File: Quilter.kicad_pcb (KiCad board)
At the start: 2 copper layers, 62 x 56 mm, 32 parts, among them J1 IO, J2 Power, J3 Power_In, U1 SSI2144, U2 TL072

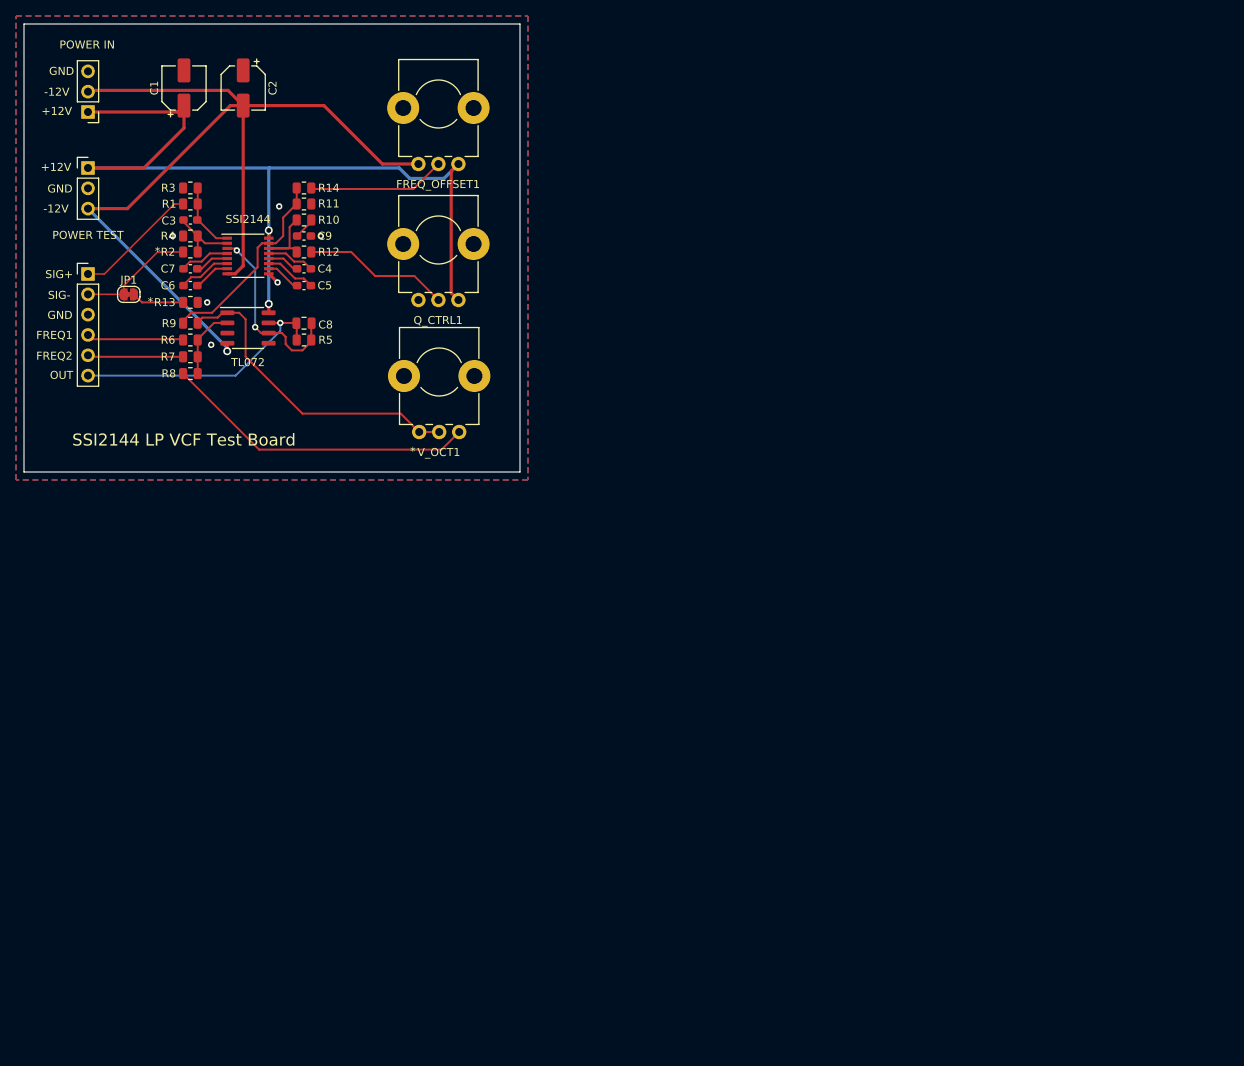
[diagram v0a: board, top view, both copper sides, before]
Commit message: Started component PCB layout
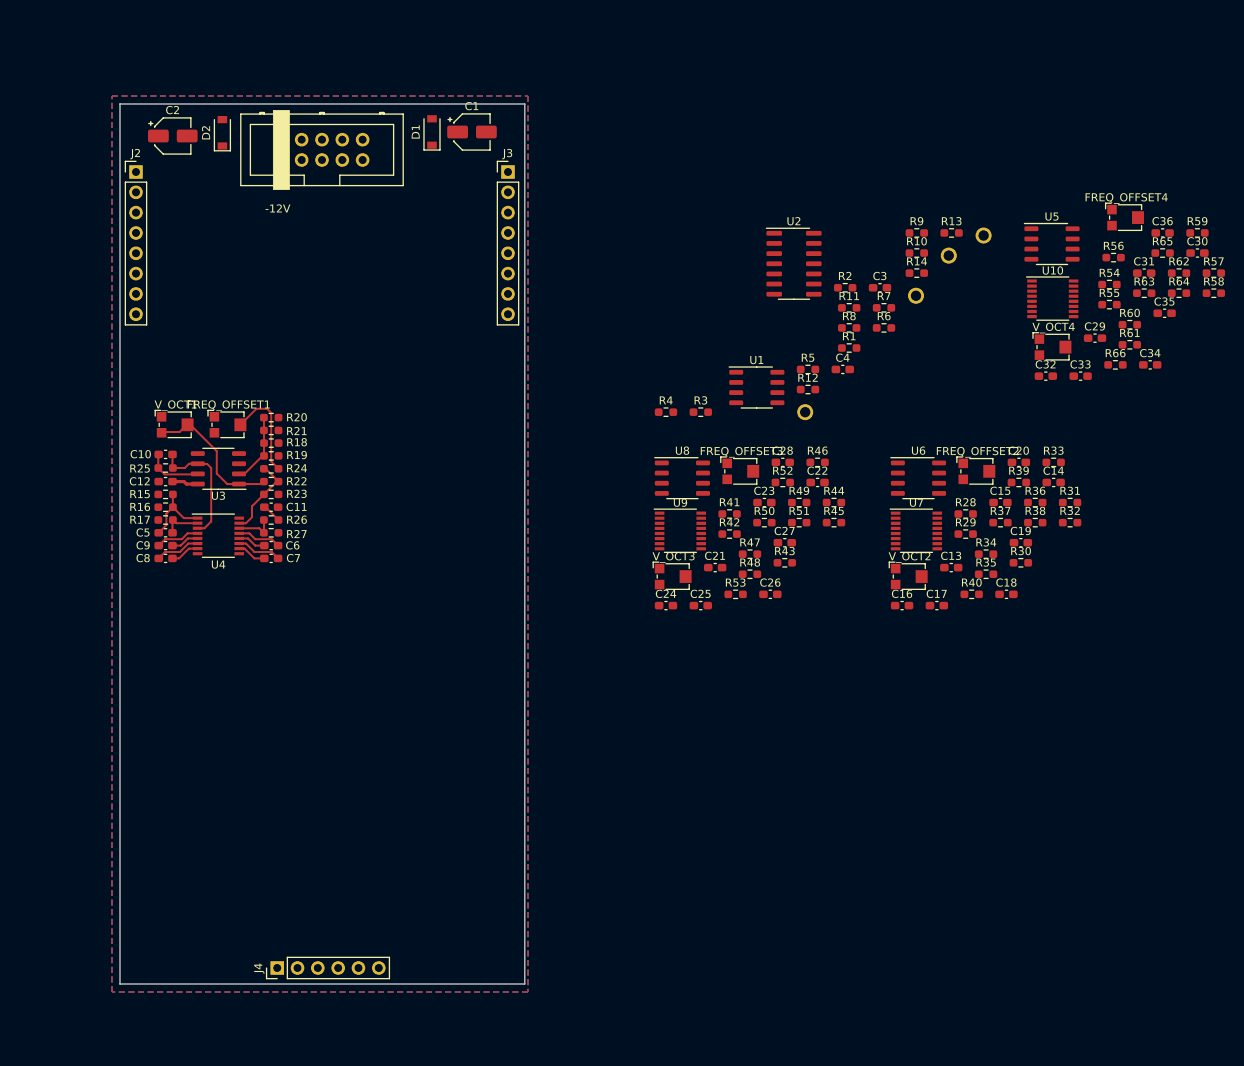
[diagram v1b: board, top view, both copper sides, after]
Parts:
- removed JP1: Jumper_2_Bridged, Jumper:SolderJumper-2_P1.3mm_Bridged_RoundedPad1.0x1.5mm
- removed Q_CTRL1: 10k, Custom_Footprints:Alpha_9mm_Potentiometer_Aligned
- added C10: 100pF, Capacitor_SMD:C_0603_1608Metric_Pad1.08x0.95mm_HandSolder, F.Cu at (55.7, 93.8)
- added C11: 10nF, Capacitor_SMD:C_0603_1608Metric_Pad1.08x0.95mm_HandSolder, F.Cu at (68.9, 100.4)
- added C12: 1uF, Capacitor_SMD:C_0603_1608Metric_Pad1.08x0.95mm_HandSolder, F.Cu at (55.7, 97.2)
- added C13: 3.3nF, Capacitor_SMD:C_0603_1608Metric_Pad1.08x0.95mm_HandSolder, F.Cu at (153.9, 108.0)
- added C14: 6.8nF, Capacitor_SMD:C_0603_1608Metric_Pad1.08x0.95mm_HandSolder, F.Cu at (166.7, 97.3)
- added C15: 6.8nF, Capacitor_SMD:C_0603_1608Metric_Pad1.08x0.95mm_HandSolder, F.Cu at (160.1, 99.8)
- added C16: 6.8nF, Capacitor_SMD:C_0603_1608Metric_Pad1.08x0.95mm_HandSolder, F.Cu at (147.8, 112.7)
- added C17: 560pF, Capacitor_SMD:C_0603_1608Metric_Pad1.08x0.95mm_HandSolder, F.Cu at (152.1, 112.7)
- added C18: 100pF, Capacitor_SMD:C_0603_1608Metric_Pad1.08x0.95mm_HandSolder, F.Cu at (160.8, 111.3)
- added C19: 10nF, Capacitor_SMD:C_0603_1608Metric_Pad1.08x0.95mm_HandSolder, F.Cu at (162.6, 104.8)
- added C20: 1uF, Capacitor_SMD:C_0603_1608Metric_Pad1.08x0.95mm_HandSolder, F.Cu at (162.4, 94.8)
- added C21: 3.3nF, Capacitor_SMD:C_0603_1608Metric_Pad1.08x0.95mm_HandSolder, F.Cu at (124.4, 108.0)
- added C22: 6.8nF, Capacitor_SMD:C_0603_1608Metric_Pad1.08x0.95mm_HandSolder, F.Cu at (137.2, 97.3)
- added C23: 6.8nF, Capacitor_SMD:C_0603_1608Metric_Pad1.08x0.95mm_HandSolder, F.Cu at (130.6, 99.8)
- added C24: 6.8nF, Capacitor_SMD:C_0603_1608Metric_Pad1.08x0.95mm_HandSolder, F.Cu at (118.2, 112.7)
- added C25: 560pF, Capacitor_SMD:C_0603_1608Metric_Pad1.08x0.95mm_HandSolder, F.Cu at (122.6, 112.7)
- added C26: 100pF, Capacitor_SMD:C_0603_1608Metric_Pad1.08x0.95mm_HandSolder, F.Cu at (131.3, 111.3)
- added C27: 10nF, Capacitor_SMD:C_0603_1608Metric_Pad1.08x0.95mm_HandSolder, F.Cu at (133.1, 104.8)
- added C28: 1uF, Capacitor_SMD:C_0603_1608Metric_Pad1.08x0.95mm_HandSolder, F.Cu at (132.8, 94.8)
- added C29: 3.3nF, Capacitor_SMD:C_0603_1608Metric_Pad1.08x0.95mm_HandSolder, F.Cu at (171.9, 79.3)
- added C30: 6.8nF, Capacitor_SMD:C_0603_1608Metric_Pad1.08x0.95mm_HandSolder, F.Cu at (184.7, 68.6)
- added C31: 6.8nF, Capacitor_SMD:C_0603_1608Metric_Pad1.08x0.95mm_HandSolder, F.Cu at (178.0, 71.1)
- added C32: 6.8nF, Capacitor_SMD:C_0603_1608Metric_Pad1.08x0.95mm_HandSolder, F.Cu at (165.7, 84.0)
- added C33: 560pF, Capacitor_SMD:C_0603_1608Metric_Pad1.08x0.95mm_HandSolder, F.Cu at (170.1, 84.0)
- added C34: 100pF, Capacitor_SMD:C_0603_1608Metric_Pad1.08x0.95mm_HandSolder, F.Cu at (178.8, 82.6)
- added C35: 10nF, Capacitor_SMD:C_0603_1608Metric_Pad1.08x0.95mm_HandSolder, F.Cu at (180.6, 76.2)
- added C36: 1uF, Capacitor_SMD:C_0603_1608Metric_Pad1.08x0.95mm_HandSolder, F.Cu at (180.3, 66.1)
- added D1: 1N5819, Diode_SMD:D_SOD-123, F.Cu at (89.0, 53.5)
- added D2: 1N5819, Diode_SMD:D_SOD-123, F.Cu at (62.8, 53.6)
- added FREQ_OFFSET2: 50k, Potentiometer_SMD:Potentiometer_Bourns_TC33X_Vertical, F.Cu at (157.2, 95.9)
- added FREQ_OFFSET3: 50k, Potentiometer_SMD:Potentiometer_Bourns_TC33X_Vertical, F.Cu at (127.7, 95.9)
- added FREQ_OFFSET4: 50k, Potentiometer_SMD:Potentiometer_Bourns_TC33X_Vertical, F.Cu at (175.8, 64.2)
- added J4: IO, Connector_PinHeader_2.54mm:PinHeader_1x06_P2.54mm_Vertical, F.Cu at (69.7, 158.0)
- added R15: 68.1k, Resistor_SMD:R_0603_1608Metric_Pad0.98x0.95mm_HandSolder, F.Cu at (55.7, 98.8)
- added R16: 200, Resistor_SMD:R_0603_1608Metric_Pad0.98x0.95mm_HandSolder, F.Cu at (55.7, 100.4)
- added R17: 200, Resistor_SMD:R_0603_1608Metric_Pad0.98x0.95mm_HandSolder, F.Cu at (55.7, 102.0)
- added R18: 100k, Resistor_SMD:R_0603_1608Metric_Pad0.98x0.95mm_HandSolder, F.Cu at (68.9, 92.4)
- added R19: 100k, Resistor_SMD:R_0603_1608Metric_Pad0.98x0.95mm_HandSolder, F.Cu at (68.9, 94.0)
- added R20: 100k, Resistor_SMD:R_0603_1608Metric_Pad0.98x0.95mm_HandSolder, F.Cu at (68.9, 89.2)
- added R21: 162k, Resistor_SMD:R_0603_1608Metric_Pad0.98x0.95mm_HandSolder, F.Cu at (68.9, 90.8)
- added R22: 100k, Resistor_SMD:R_0603_1608Metric_Pad0.98x0.95mm_HandSolder, F.Cu at (68.9, 97.2)
- added R23: 1k, Resistor_SMD:R_0603_1608Metric_Pad0.98x0.95mm_HandSolder, F.Cu at (68.9, 98.8)
- added R24: 499k, Resistor_SMD:R_0603_1608Metric_Pad0.98x0.95mm_HandSolder, F.Cu at (68.9, 95.6)
- added R25: 33.2k, Resistor_SMD:R_0603_1608Metric_Pad0.98x0.95mm_HandSolder, F.Cu at (55.7, 95.5)
- added R26: 499, Resistor_SMD:R_0603_1608Metric_Pad0.98x0.95mm_HandSolder, F.Cu at (68.9, 102.0)
- added R27: 26.7k, Resistor_SMD:R_0603_1608Metric_Pad0.98x0.95mm_HandSolder, F.Cu at (68.9, 103.6)
- added R28: 68.1k, Resistor_SMD:R_0603_1608Metric_Pad0.98x0.95mm_HandSolder, F.Cu at (155.7, 101.2)
- added R29: 200, Resistor_SMD:R_0603_1608Metric_Pad0.98x0.95mm_HandSolder, F.Cu at (155.7, 103.8)
- added R30: 200, Resistor_SMD:R_0603_1608Metric_Pad0.98x0.95mm_HandSolder, F.Cu at (162.6, 107.3)
- added R31: 100k, Resistor_SMD:R_0603_1608Metric_Pad0.98x0.95mm_HandSolder, F.Cu at (168.8, 99.8)
- added R32: 100k, Resistor_SMD:R_0603_1608Metric_Pad0.98x0.95mm_HandSolder, F.Cu at (168.8, 102.3)
- added R33: 100k, Resistor_SMD:R_0603_1608Metric_Pad0.98x0.95mm_HandSolder, F.Cu at (166.7, 94.8)
- added R34: 162k, Resistor_SMD:R_0603_1608Metric_Pad0.98x0.95mm_HandSolder, F.Cu at (158.3, 106.3)
- added R35: 100k, Resistor_SMD:R_0603_1608Metric_Pad0.98x0.95mm_HandSolder, F.Cu at (158.3, 108.8)
- added R36: 1k, Resistor_SMD:R_0603_1608Metric_Pad0.98x0.95mm_HandSolder, F.Cu at (164.4, 99.8)
- added R37: 499k, Resistor_SMD:R_0603_1608Metric_Pad0.98x0.95mm_HandSolder, F.Cu at (160.1, 102.3)
- added R38: 33.2k, Resistor_SMD:R_0603_1608Metric_Pad0.98x0.95mm_HandSolder, F.Cu at (164.4, 102.3)
- added R39: 499, Resistor_SMD:R_0603_1608Metric_Pad0.98x0.95mm_HandSolder, F.Cu at (162.4, 97.3)
- added R40: 26.7k, Resistor_SMD:R_0603_1608Metric_Pad0.98x0.95mm_HandSolder, F.Cu at (156.5, 111.3)
- added R41: 68.1k, Resistor_SMD:R_0603_1608Metric_Pad0.98x0.95mm_HandSolder, F.Cu at (126.2, 101.2)
- added R42: 200, Resistor_SMD:R_0603_1608Metric_Pad0.98x0.95mm_HandSolder, F.Cu at (126.2, 103.8)
- added R43: 200, Resistor_SMD:R_0603_1608Metric_Pad0.98x0.95mm_HandSolder, F.Cu at (133.1, 107.3)
- added R44: 100k, Resistor_SMD:R_0603_1608Metric_Pad0.98x0.95mm_HandSolder, F.Cu at (139.2, 99.8)
- added R45: 100k, Resistor_SMD:R_0603_1608Metric_Pad0.98x0.95mm_HandSolder, F.Cu at (139.2, 102.3)
- added R46: 100k, Resistor_SMD:R_0603_1608Metric_Pad0.98x0.95mm_HandSolder, F.Cu at (137.2, 94.8)
- added R47: 162k, Resistor_SMD:R_0603_1608Metric_Pad0.98x0.95mm_HandSolder, F.Cu at (128.8, 106.3)
- added R48: 100k, Resistor_SMD:R_0603_1608Metric_Pad0.98x0.95mm_HandSolder, F.Cu at (128.8, 108.8)
- added R49: 1k, Resistor_SMD:R_0603_1608Metric_Pad0.98x0.95mm_HandSolder, F.Cu at (134.9, 99.8)
- added R50: 499k, Resistor_SMD:R_0603_1608Metric_Pad0.98x0.95mm_HandSolder, F.Cu at (130.6, 102.3)
- added R51: 33.2k, Resistor_SMD:R_0603_1608Metric_Pad0.98x0.95mm_HandSolder, F.Cu at (134.9, 102.3)
- added R52: 499, Resistor_SMD:R_0603_1608Metric_Pad0.98x0.95mm_HandSolder, F.Cu at (132.8, 97.3)
- added R53: 26.7k, Resistor_SMD:R_0603_1608Metric_Pad0.98x0.95mm_HandSolder, F.Cu at (127.0, 111.3)
- added R54: 68.1k, Resistor_SMD:R_0603_1608Metric_Pad0.98x0.95mm_HandSolder, F.Cu at (173.7, 72.6)
- added R55: 200, Resistor_SMD:R_0603_1608Metric_Pad0.98x0.95mm_HandSolder, F.Cu at (173.7, 75.1)
- added R56: 200, Resistor_SMD:R_0603_1608Metric_Pad0.98x0.95mm_HandSolder, F.Cu at (174.2, 69.2)
- added R57: 100k, Resistor_SMD:R_0603_1608Metric_Pad0.98x0.95mm_HandSolder, F.Cu at (186.7, 71.1)
- added R58: 100k, Resistor_SMD:R_0603_1608Metric_Pad0.98x0.95mm_HandSolder, F.Cu at (186.7, 73.7)
- added R59: 100k, Resistor_SMD:R_0603_1608Metric_Pad0.98x0.95mm_HandSolder, F.Cu at (184.7, 66.1)
- added R60: 162k, Resistor_SMD:R_0603_1608Metric_Pad0.98x0.95mm_HandSolder, F.Cu at (176.2, 77.6)
- added R61: 100k, Resistor_SMD:R_0603_1608Metric_Pad0.98x0.95mm_HandSolder, F.Cu at (176.2, 80.1)
- added R62: 1k, Resistor_SMD:R_0603_1608Metric_Pad0.98x0.95mm_HandSolder, F.Cu at (182.4, 71.1)
- added R63: 499k, Resistor_SMD:R_0603_1608Metric_Pad0.98x0.95mm_HandSolder, F.Cu at (178.0, 73.7)
- added R64: 33.2k, Resistor_SMD:R_0603_1608Metric_Pad0.98x0.95mm_HandSolder, F.Cu at (182.4, 73.7)
- added R65: 499, Resistor_SMD:R_0603_1608Metric_Pad0.98x0.95mm_HandSolder, F.Cu at (180.3, 68.6)
- added R66: 26.7k, Resistor_SMD:R_0603_1608Metric_Pad0.98x0.95mm_HandSolder, F.Cu at (174.4, 82.6)
- added TP1: TestPoint, Custom_Footprints:1.3mm_Test_Point, F.Cu at (135.7, 88.5)
- added TP2: TestPoint, Custom_Footprints:1.3mm_Test_Point, F.Cu at (157.9, 66.4)
- added TP3: TestPoint, Custom_Footprints:1.3mm_Test_Point, F.Cu at (153.6, 69.0)
- added TP4: TestPoint, Custom_Footprints:1.3mm_Test_Point, F.Cu at (149.5, 74.0)
- added U10: SSI2144, Package_SO:SSOP-16_3.9x4.9mm_P0.635mm, F.Cu at (166.6, 74.3)
- added U3: TL072, Package_SO:SO-8_3.9x4.9mm_P1.27mm, F.Cu at (62.3, 95.6)
- added U4: SSI2144, Package_SO:SSOP-16_3.9x4.9mm_P0.635mm, F.Cu at (62.3, 104.0)
- added U5: TL072, Package_SO:SO-8_3.9x4.9mm_P1.27mm, F.Cu at (166.5, 67.5)
- added U6: TL072, Package_SO:SO-8_3.9x4.9mm_P1.27mm, F.Cu at (149.8, 96.8)
- added U7: SSI2144, Package_SO:SSOP-16_3.9x4.9mm_P0.635mm, F.Cu at (149.6, 103.4)
- added U8: TL072, Package_SO:SO-8_3.9x4.9mm_P1.27mm, F.Cu at (120.3, 96.8)
- added U9: SSI2144, Package_SO:SSOP-16_3.9x4.9mm_P0.635mm, F.Cu at (120.0, 103.4)
- added V_OCT2: 50k, Potentiometer_SMD:Potentiometer_Bourns_TC33X_Vertical, F.Cu at (148.8, 109.1)
- added V_OCT3: 50k, Potentiometer_SMD:Potentiometer_Bourns_TC33X_Vertical, F.Cu at (119.2, 109.1)
- added V_OCT4: 50k, Potentiometer_SMD:Potentiometer_Bourns_TC33X_Vertical, F.Cu at (166.7, 80.4)
- C1, C2: footprint Capacitor_SMD:CP_Elec_5x5.7 -> Capacitor_SMD:CP_Elec_4x5.8
- C3: value 3.3nF -> 1uF
- C4: value 6.8nF -> 1uF
- C5: value 6.8nF -> 3.3nF
- C7: value 560pF -> 6.8nF
- C8: value 100pF -> 6.8nF; footprint Capacitor_SMD:C_0805_2012Metric -> Capacitor_SMD:C_0603_1608Metric_Pad1.08x0.95mm_HandSolder
- FREQ_OFFSET1, V_OCT1: footprint Custom_Footprints:Alpha_9mm_Potentiometer_Aligned -> Potentiometer_SMD:Potentiometer_Bourns_TC33X_Vertical
- J1: value IO -> Eurorack_10_pin_power; footprint Connector_PinHeader_2.54mm:PinHeader_1x06_P2.54mm_Vertical -> Custom_Footprints:Eurorack_10_pin_header
- J2: value Power -> Conn_01x08_Male; footprint Connector_PinHeader_2.54mm:PinHeader_1x03_P2.54mm_Vertical -> Connector_PinHeader_2.54mm:PinHeader_1x08_P2.54mm_Vertical
- J3: value Power_In -> Conn_01x08_Male; footprint Connector_PinHeader_2.54mm:PinHeader_1x03_P2.54mm_Vertical -> Connector_PinHeader_2.54mm:PinHeader_1x08_P2.54mm_Vertical
- R1: value 68.1k -> 14k; footprint Resistor_SMD:R_0805_2012Metric -> Resistor_SMD:R_0603_1608Metric_Pad0.98x0.95mm_HandSolder
- R10: value 499 -> 10k; footprint Resistor_SMD:R_0805_2012Metric -> Resistor_SMD:R_0603_1608Metric_Pad0.98x0.95mm_HandSolder
- R11: value 1k -> 10k; footprint Resistor_SMD:R_0805_2012Metric -> Resistor_SMD:R_0603_1608Metric_Pad0.98x0.95mm_HandSolder
- R12: value 26.7k -> 10k; footprint Resistor_SMD:R_0805_2012Metric -> Resistor_SMD:R_0603_1608Metric_Pad0.98x0.95mm_HandSolder
- R13, R3, R4: value 200 -> 10k; footprint Resistor_SMD:R_0805_2012Metric -> Resistor_SMD:R_0603_1608Metric_Pad0.98x0.95mm_HandSolder
- R14: value 499k -> 10k; footprint Resistor_SMD:R_0805_2012Metric -> Resistor_SMD:R_0603_1608Metric_Pad0.98x0.95mm_HandSolder
- R2, R6, R7, R9: value 100k -> 10k; footprint Resistor_SMD:R_0805_2012Metric -> Resistor_SMD:R_0603_1608Metric_Pad0.98x0.95mm_HandSolder
- R5: value 33.2k -> 10k; footprint Resistor_SMD:R_0805_2012Metric -> Resistor_SMD:R_0603_1608Metric_Pad0.98x0.95mm_HandSolder
- R8: value 162k -> 10k; footprint Resistor_SMD:R_0805_2012Metric -> Resistor_SMD:R_0603_1608Metric_Pad0.98x0.95mm_HandSolder
- U1: value SSI2144 -> TL072; footprint Package_SO:SSOP-16_3.9x4.9mm_P0.635mm -> Package_SO:SO-8_3.9x4.9mm_P1.27mm
- U2: value TL072 -> TL074; footprint Package_SO:SO-8_3.9x4.9mm_P1.27mm -> Package_SO:SOIC-14_3.9x8.7mm_P1.27mm
- moved R13 95.5 mm to (153.9, 66.1), turned to 0 degrees
- moved R9 91.5 mm to (149.6, 66.1)
- moved R7 86.9 mm to (145.5, 75.5), turned to 0 degrees
- moved R6 86.7 mm to (145.5, 78.0), turned to 0 degrees
- moved C3 86.6 mm to (145.0, 73.0)
- moved R1 84.3 mm to (141.2, 80.5), turned to 0 degrees
- moved R8 82.5 mm to (141.2, 78.0)
- moved R2 82.0 mm to (140.7, 73.0), turned to 0 degrees
- moved R14 77.3 mm to (149.6, 71.1)
- moved R10 76.7 mm to (149.6, 68.6), turned to 0 degrees
- moved R3 69.7 mm to (122.6, 88.5)
- moved R11 69.4 mm to (141.2, 75.5)
- moved U2 68.7 mm to (134.2, 70.0)
- moved C4 68.5 mm to (140.3, 83.2), turned to 0 degrees
- moved U1 65.7 mm to (129.6, 85.4)
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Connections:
- C3 pad 1: Net-(C3-Pad1) -> +12V
- C3 pad 2: Net-(C3-Pad2) -> GND
- C4 pad 1: Net-(C4-Pad1) -> +12V
- C4 pad 2: Net-(C4-Pad2) -> GND
- C8 pad 1: /MIX_OUT -> Net-(C8-Pad1)
- C9 pad 2: GND -> Net-(C9-Pad2)
- J1 pad 1: /SIG_IN+ -> /-12V_IN
- J1 pad 2: /SIG_IN- -> /-12V_IN
- J1 pad 4: /FREQ1 -> GND
- J1 pad 5: /FREQ2 -> GND
- J1 pad 6: /MIX_OUT -> GND
- J2 pad 1: +12V -> /AUDIO_IN1
- J2 pad 2: GND -> /FREQ_CV1
- J2 pad 3: -12V -> /FREQ_V_OCT1
- J3 pad 1: +12V -> /AUDIO_IN2
- J3 pad 2: -12V -> /FREQ_CV2
- J3 pad 3: GND -> /FREQ_V_OCT2
- R1 pad 1: Net-(C3-Pad2) -> +12V
- R1 pad 2: /SIG_IN+ -> /FREQ_POT_5V
- R10 pad 1: Net-(C9-Pad1) -> Net-(R10-Pad1)
- R10 pad 2: /Q_CTRL -> /Audio_Out4
- R11 pad 1: /FREQ_CTRL -> /AUDIO_BUFF1
- R11 pad 2: GND -> Net-(R11-Pad2)
- R12 pad 1: Net-(R12-Pad1) -> /AUDIO_BUFF2
- R12 pad 2: /Q_CTRL -> Net-(R12-Pad2)
- R13 pad 1: GND -> /AUDIO_BUFF3
- R13 pad 2: Net-(JP1-Pad2) -> Net-(R13-Pad2)
- R14 pad 1: /FREQ_CTRL -> /AUDIO_BUFF4
- R14 pad 2: Net-(FREQ_OFFSET1-Pad2) -> Net-(R10-Pad1)
- R2 pad 1: Net-(C3-Pad1) -> Net-(R2-Pad1)
- R2 pad 2: /SIG_IN- -> /Audio_Out1
- R3 pad 1: GND -> Net-(R2-Pad1)
- R3 pad 2: Net-(C3-Pad2) -> /Audio_Out2
- R4 pad 1: Net-(C3-Pad1) -> Net-(R2-Pad1)
- R4 pad 2: GND -> /Audio_Out3
- R5 pad 1: /MIX_OUT -> Net-(R2-Pad1)
- R5 pad 2: Net-(C8-Pad2) -> /Audio_Out4
- R6 pad 1: Net-(R6-Pad1) -> /AUDIO_MIX
- R6 pad 2: /FREQ1 -> Net-(R2-Pad1)
- R7 pad 1: Net-(R6-Pad1) -> Net-(R11-Pad2)
- R7 pad 2: /FREQ2 -> /Audio_Out1
- R8 pad 1: Net-(R8-Pad1) -> Net-(R12-Pad2)
- R8 pad 2: Net-(R6-Pad1) -> /Audio_Out2
- R9 pad 1: /FREQ_CTRL -> Net-(R13-Pad2)
- R9 pad 2: Net-(R9-Pad2) -> /Audio_Out3
- U1 pad 1: Net-(C3-Pad2) -> /AUDIO_MIX
- U1 pad 2: Net-(C3-Pad1) -> Net-(R2-Pad1)
- U1 pad 3: Net-(C8-Pad2) -> GND
- U1 pad 4: Net-(C7-Pad1) -> -12V
- U1 pad 5: Net-(C7-Pad2) -> GND
- U1 pad 6: Net-(C6-Pad1) -> Net-(U1-Pad6)
- U1 pad 7: Net-(C6-Pad2) -> Net-(U1-Pad6)
- U1 pad 8: -12V -> +12V
- U2 pad 1: Net-(R9-Pad2) -> /AUDIO_BUFF1
- U2 pad 2: Net-(R6-Pad1) -> Net-(R11-Pad2)
- U2 pad 4: -12V -> +12V
- U2 pad 6: Net-(C8-Pad2) -> Net-(R12-Pad2)
- U2 pad 7: /MIX_OUT -> /AUDIO_BUFF2
- U2 pad 8: +12V -> /AUDIO_BUFF3
- V_OCT1 pad 1: Net-(R8-Pad1) -> Net-(R21-Pad1)
- V_OCT1 pad 2: Net-(R9-Pad2) -> Net-(R22-Pad2)
- V_OCT1 pad 3: Net-(R9-Pad2) -> Net-(R22-Pad2)
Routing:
- net -12V: track 118.7 -> 0.00 mm, vias 1 -> 0
- net +12V: track 113.7 -> 3.29 mm, vias 2 -> 0
- net Net-(R9-Pad2): track 39.7 -> 0.00 mm
- net Net-(R8-Pad1): track 39.4 -> 0.00 mm
- net /MIX_OUT: track 33.1 -> 0.00 mm, vias 1 -> 0
- net /FREQ_CTRL: track 25.3 -> 0.00 mm
- net Net-(C8-Pad2): track 23.4 -> 3.64 mm, vias 2 -> 0
- net Net-(R12-Pad1): track 18.4 -> 0.00 mm
- net Net-(R22-Pad2): track 0.00 -> 18.1 mm
- net Net-(C10-Pad2): track 0.00 -> 15.7 mm
- net /SIG_IN+: track 15.5 -> 0.00 mm
- net /SIG_IN-: track 14.7 -> 0.00 mm
- net /FREQ1: track 12.1 -> 0.00 mm
- net /FREQ2: track 12.0 -> 0.00 mm
- net /Filter_Voice1/FREQ_CTRL: track 0.00 -> 10.4 mm
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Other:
- board size 62 x 56 mm -> 50.6 x 110 mm
- board text removed: "*"
- board text removed: "+12V"
- board text removed: "-12V"
- board text removed: "FREQ1"
- board text removed: "FREQ2"
- board text removed: "GND"
- board text removed: "OUT"
- board text removed: "POWER IN"
- board text removed: "POWER TEST"
- board text removed: "SIG+"
- board text removed: "SIG-"
- board text removed: "SSI2144"
- board text removed: "SSI2144 LP VCF Test Board"
- board text removed: "TL072"

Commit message: First draft of component PCB routed
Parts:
- added C37: 1uF, Capacitor_SMD:C_0603_1608Metric_Pad1.08x0.95mm_HandSolder, F.Cu at (68.4, 82.6)
- added C38: 1uF, Capacitor_SMD:C_0603_1608Metric_Pad1.08x0.95mm_HandSolder, F.Cu at (81.6, 69.7)
- added C39: 1uF, Capacitor_SMD:C_0603_1608Metric_Pad1.08x0.95mm_HandSolder, F.Cu at (55.7, 108.4)
- added C40: 1uF, Capacitor_SMD:C_0603_1608Metric_Pad1.08x0.95mm_HandSolder, F.Cu at (68.9, 100.4)
- added C41: 1uF, Capacitor_SMD:C_0603_1608Metric_Pad1.08x0.95mm_HandSolder, F.Cu at (81.6, 108.4)
- added C42: 1uF, Capacitor_SMD:C_0603_1608Metric_Pad1.08x0.95mm_HandSolder, F.Cu at (94.8, 100.4)
- added C43: 1uF, Capacitor_SMD:C_0603_1608Metric_Pad1.08x0.95mm_HandSolder, F.Cu at (55.7, 136.2)
- added C44: 1uF, Capacitor_SMD:C_0603_1608Metric_Pad1.08x0.95mm_HandSolder, F.Cu at (68.9, 128.2)
- added C45: 1uF, Capacitor_SMD:C_0603_1608Metric_Pad1.08x0.95mm_HandSolder, F.Cu at (81.6, 136.2)
- added C46: 1uF, Capacitor_SMD:C_0603_1608Metric_Pad1.08x0.95mm_HandSolder, F.Cu at (94.8, 128.2)
- J2, J3: footprint Connector_PinHeader_2.54mm:PinHeader_1x08_P2.54mm_Vertical -> Connector_PinHeader_2.54mm:PinHeader_1x10_P2.54mm_Vertical; moved to B.Cu
- J4: footprint Connector_PinHeader_2.54mm:PinHeader_1x06_P2.54mm_Vertical -> Connector_PinHeader_2.54mm:PinHeader_1x10_P2.54mm_Vertical; moved to B.Cu
- moved TP3 143.5 mm to (49.0, 167.2)
- moved C36 115.0 mm to (81.6, 125.0), turned to 180 degrees
- moved R64 112.3 mm to (81.6, 123.3)
- moved C30 111.5 mm to (94.8, 134.6), turned to 180 degrees
- moved R56 110.7 mm to (81.6, 129.8), turned to 180 degrees
- moved R54 106.8 mm to (81.6, 126.6), turned to 180 degrees
- moved R55 106.3 mm to (81.6, 128.2)
- moved R65 106.1 mm to (94.8, 131.4), turned to 180 degrees
- moved C31 105.6 mm to (94.8, 136.2), turned to 180 degrees
- moved C34 104.7 mm to (81.6, 121.6)
- moved C29 104.2 mm to (81.6, 131.4), turned to 180 degrees
- moved R57 104.2 mm to (94.8, 120.2)
- moved R59 104.1 mm to (94.8, 118.6)
- moved R58 103.8 mm to (94.8, 121.8)
- moved R62 103.7 mm to (94.8, 126.6)
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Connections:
- J2 pad 1: /AUDIO_IN1 -> unconnected-(J2-Pad1)
- J2 pad 2: /FREQ_CV1 -> unconnected-(J2-Pad2)
- J2 pad 3: /FREQ_V_OCT1 -> unconnected-(J2-Pad3)
- J2 pad 4: /AUDIO_BUFF1 -> /FREQ_V_OCT1
- J2 pad 5: GND -> /AUDIO_BUFF1
- J2 pad 6: /AUDIO_IN3 -> GND
- J2 pad 7: /FREQ_CV3 -> unconnected-(J2-Pad7)
- J2 pad 8: /FREQ_V_OCT3 -> /AUDIO_BUFF4
- J3 pad 1: /AUDIO_IN2 -> unconnected-(J3-Pad1)
- J3 pad 2: /FREQ_CV2 -> /AUDIO_BUFF3
- J3 pad 3: /FREQ_V_OCT2 -> /AUDIO_BUFF2
- J3 pad 4: /AUDIO_BUFF2 -> /FREQ_V_OCT2
- J3 pad 5: GND -> unconnected-(J3-Pad5)
- J3 pad 6: /AUDIO_BUFF3 -> GND
- J3 pad 7: /AUDIO_IN4 -> unconnected-(J3-Pad7)
- J3 pad 8: /AUDIO_BUFF4 -> /FREQ_CV2
- J4 pad 1: /FREQ_CV4 -> unconnected-(J4-Pad1)
- J4 pad 3: /FREQ_POT -> /FREQ_CV4
- J4 pad 5: /FREQ_POT_5V -> /AUDIO_IN4
- J4 pad 6: /AUDIO_MIX -> /FREQ_CV1
- R10 pad 2: /Audio_Out4 -> /Audio_Out2
- R12 pad 1: /AUDIO_BUFF2 -> /AUDIO_BUFF3
- R13 pad 1: /AUDIO_BUFF3 -> /AUDIO_BUFF4
- R14 pad 1: /AUDIO_BUFF4 -> /AUDIO_BUFF2
- R8 pad 2: /Audio_Out2 -> /Audio_Out3
- R9 pad 2: /Audio_Out3 -> /Audio_Out4
- U2 pad 11: GND -> -12V
- U2 pad 14: /AUDIO_BUFF4 -> /AUDIO_BUFF2
- U2 pad 7: /AUDIO_BUFF2 -> /AUDIO_BUFF3
- U2 pad 8: /AUDIO_BUFF3 -> /AUDIO_BUFF4
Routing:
- net -12V: track 0.00 -> 275.3 mm, vias 0 -> 11
- net +12V: track 3.29 -> 259.5 mm, vias 0 -> 14
- net /Q_POT: track 0.00 -> 163.5 mm, vias 0 -> 4
- net /FREQ_POT: track 0.00 -> 153.3 mm, vias 0 -> 2
- net /FREQ_V_OCT3: track 0.00 -> 71.0 mm
- net /FREQ_CV1: track 0.00 -> 68.1 mm
- net /Audio_Out3: track 0.00 -> 66.6 mm, vias 0 -> 2
- net /AUDIO_IN2: track 0.00 -> 64.5 mm
- net /Audio_Out4: track 0.00 -> 63.0 mm
- net /FREQ_V_OCT4: track 0.00 -> 46.6 mm
- net /FREQ_CV4: track 0.00 -> 43.6 mm
- net /Audio_Out1: track 7.22 -> 50.8 mm
- net /FREQ_V_OCT1: track 0.00 -> 40.9 mm, vias 0 -> 1
- net /Audio_Out2: track 0.00 -> 39.5 mm
- net /AUDIO_BUFF3: track 0.00 -> 38.9 mm
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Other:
- board text added: "Freq Offset"
- board text added: "V/Oct"

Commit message: Started Controls PCB
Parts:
- renumbered C5 to C37, C8 to C38, C37 to C5, C38 to C8, J2 to J1, J3 to J2, J4 to J3, J1 to J4
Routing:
- net +12V: track 259.5 -> 267.5 mm
- net -12V: track 275.3 -> 276.7 mm
- net /Audio_Out1: track 50.8 -> 49.4 mm
- net /FREQ_POT: track 153.3 -> 154.5 mm
- net /AUDIO_IN1: track 18.8 -> 19.8 mm
- net /Q_POT: track 163.5 -> 162.9 mm
